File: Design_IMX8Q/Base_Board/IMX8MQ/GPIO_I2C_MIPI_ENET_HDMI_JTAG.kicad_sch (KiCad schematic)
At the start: 1 part, among them U1 MIMX8MQ6CVAHZAB

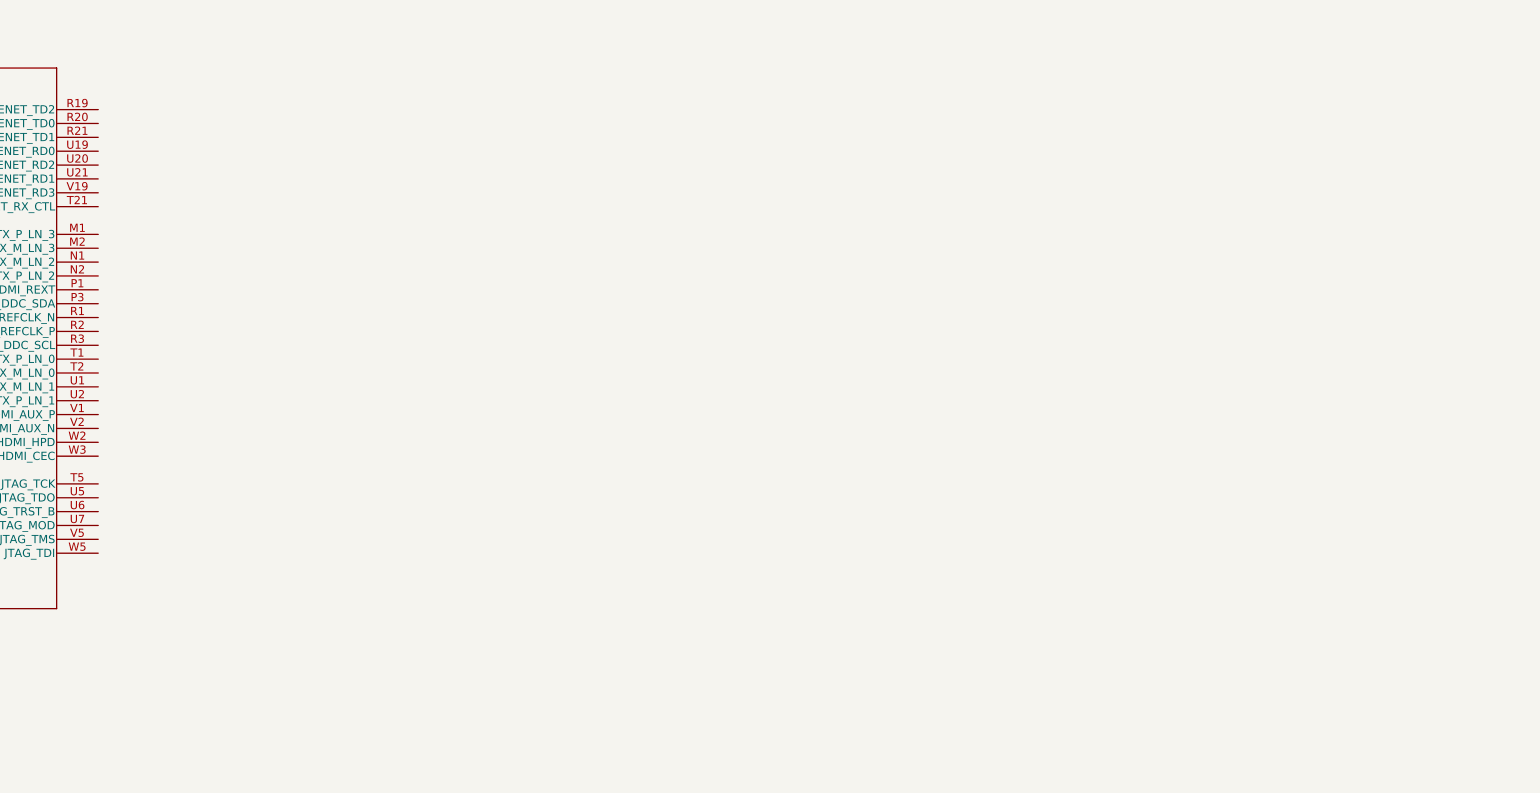
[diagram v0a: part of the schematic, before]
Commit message: changes vias pad size
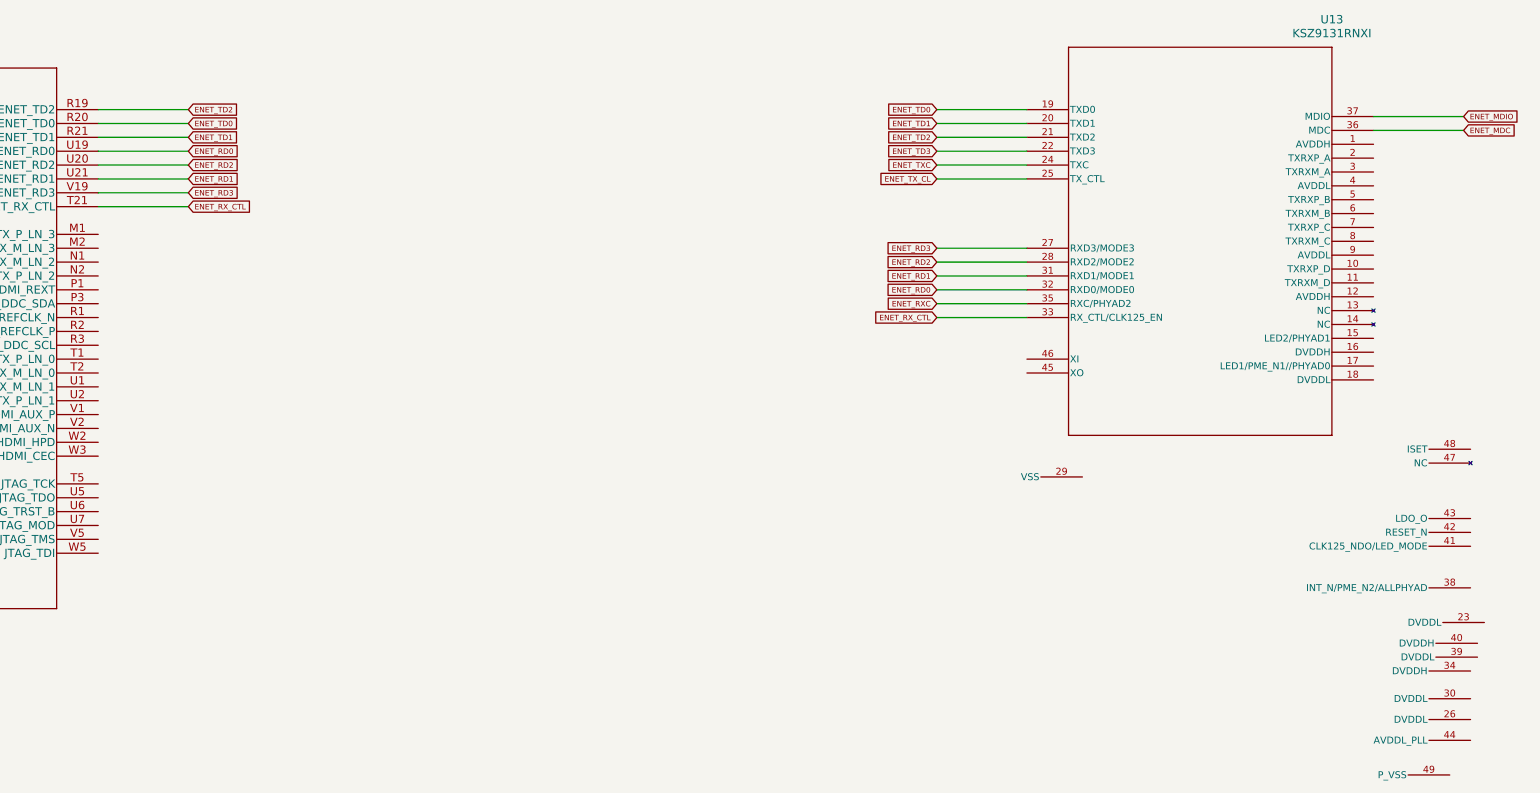
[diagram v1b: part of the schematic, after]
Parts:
- added U13: KSZ9131RNXI, Package_DFN_QFN:VQFN-48-1EP_7x7mm_P0.5mm_EP5.15x5.15mm, symbol KSZ9131RNXI:KSZ9131RNXI
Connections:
- net ENET_TD2: now reaches U1.R19 (ENET_TD2)
- net ENET_TD2: now also U13.21 (TXD2)
- net ENET_TD0: now reaches U1.R20 (ENET_TD0)
- net ENET_TD0: now also U13.19 (TXD0)
- net ENET_TD1: now reaches U1.R21 (ENET_TD1)
- net ENET_TD1: now also U13.20 (TXD1)
- net ENET_RX_CTL: now reaches U1.T21 (ENET_RX_CTL)
- net ENET_RX_CTL: now also U13.33 (RX_CTL/CLK125_EN)
- net ENET_RD0: now reaches U1.U19 (ENET_RD0)
- net ENET_RD0: now also U13.32 (RXD0/MODE0)
- net ENET_RD2: now reaches U1.U20 (ENET_RD2)
- net ENET_RD2: now also U13.28 (RXD2/MODE2)
- net ENET_RD1: now reaches U1.U21 (ENET_RD1)
- net ENET_RD1: now also U13.31 (RXD1/MODE1)
- net ENET_RD3: now reaches U1.V19 (ENET_RD3)
- net ENET_RD3: now also U13.27 (RXD3/MODE3)
- new net ENET_MDC: U13.36 (MDC)
- new net ENET_MDIO: U13.37 (MDIO)
- new net ENET_RXC: U13.35 (RXC/PHYAD2)
- new net ENET_TD3: U13.22 (TXD3)
- new net ENET_TXC: U13.24 (TXC)
- new net ENET_TX_CL: U13.25 (TX_CTL)

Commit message: Update IMX6QP and IMX8MQ
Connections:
- net MIPI_CSI2_CLK-: now reaches U1.A19 (MIPI_CSI2_CLK_N)
- net MIPI_CSI1_CLK-: now reaches U1.A22 (MIPI_CSI1_CLK_N)
- net MIPI_CSI2_CLK+: now reaches U1.B19 (MIPI_CSI2_CLK_P)
- net MIPI_CSI1_CLK+: now reaches U1.B22 (MIPI_CSI1_CLK_P)
- net MIPI_DSI_CLK-: now reaches U1.C16 (MIPI_DSI_CLK_N)
- net MIPI_DSI_REXT: now reaches U1.C17 (MIPI_DSI_REXT)
- net MIPI_DSI_CLK+: now reaches U1.D16 (MIPI_DSI_CLK_P)
- net HDMI_TX_LN_3_+: now reaches U1.M1 (HDMI_TX_P_LN_3)
- net HDMI_TX_LN_3_-: now reaches U1.M2 (HDMI_TX_M_LN_3)
- net HDMI_TX_LN_2_-: now reaches U1.N1 (HDMI_TX_M_LN_2)
- net HDMI_TX_LN_2_+: now reaches U1.N2 (HDMI_TX_P_LN_2)
- net HDMI_REXT: now reaches U1.P1 (HDMI_REXT)
- net HDMI_DDC_SDA: now reaches U1.P3 (HDMI_DDC_SDA)
- net HDMI_REFCLK_-: now reaches U1.R1 (HDMI_REFCLK_N)
- net HDMI_REFCLK_+: now reaches U1.R2 (HDMI_REFCLK_P)
- net HDMI_DDC_SCL: now reaches U1.R3 (HDMI_DDC_SCL)
- net HDMI_TX_LN_0_+: now reaches U1.T1 (HDMI_TX_P_LN_0)
- net HDMI_TX_LN_0_-: now reaches U1.T2 (HDMI_TX_M_LN_0)
- net JTAG_TCK: now reaches U1.T5 (JTAG_TCK)
- net HDMI_TX_LN_1_-: now reaches U1.U1 (HDMI_TX_M_LN_1)
- net HDMI_TX_LN_1_+: now reaches U1.U2 (HDMI_TX_P_LN_1)
- net JTAG_TDO: now reaches U1.U5 (JTAG_TDO)
- net JTAG_TRST_B: now reaches U1.U6 (JTAG_TRST_B)
- net JTAG_MOD: now reaches U1.U7 (JTAG_MOD)
- net HDMI_AUX_+: now reaches U1.V1 (HDMI_AUX_P)
- net HDMI_AUX_-: now reaches U1.V2 (HDMI_AUX_N)
- net JTAG_TMS: now reaches U1.V5 (JTAG_TMS)
- net HDMI_HPD: now reaches U1.W2 (HDMI_HPD)
- net HDMI_CEC: now reaches U1.W3 (HDMI_CEC)
- net JTAG_TDI: now reaches U1.W5 (JTAG_TDI)

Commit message: Add QSPI and more color
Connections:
- net I2C1_SCL: now reaches U1.E7 (I2C1_SCL)
- net I2C1_SDA: now reaches U1.E8 (I2C1_SDA)
- net I2C3_SDA: now reaches U1.E9 (I2C3_SDA)
- net I2C2_SDA: now reaches U1.F7 (I2C2_SDA)
- net I2C4_SCL: now reaches U1.F8 (I2C4_SCL)
- net I2C4_SDA: now reaches U1.F9 (I2C4_SDA)
- net I2C2_SCL: now reaches U1.G7 (I2C2_SCL)
- net I2C3_SCL: now reaches U1.G8 (I2C3_SCL)
- net USB1_OTG_OC: now reaches U1.K6 (GPIO1_IO13)
- net USB1_OTG_PWR: now reaches U1.L7 (GPIO1_IO12)
- net USB1_OTG_ID: now reaches U1.M7 (GPIO1_IO10)

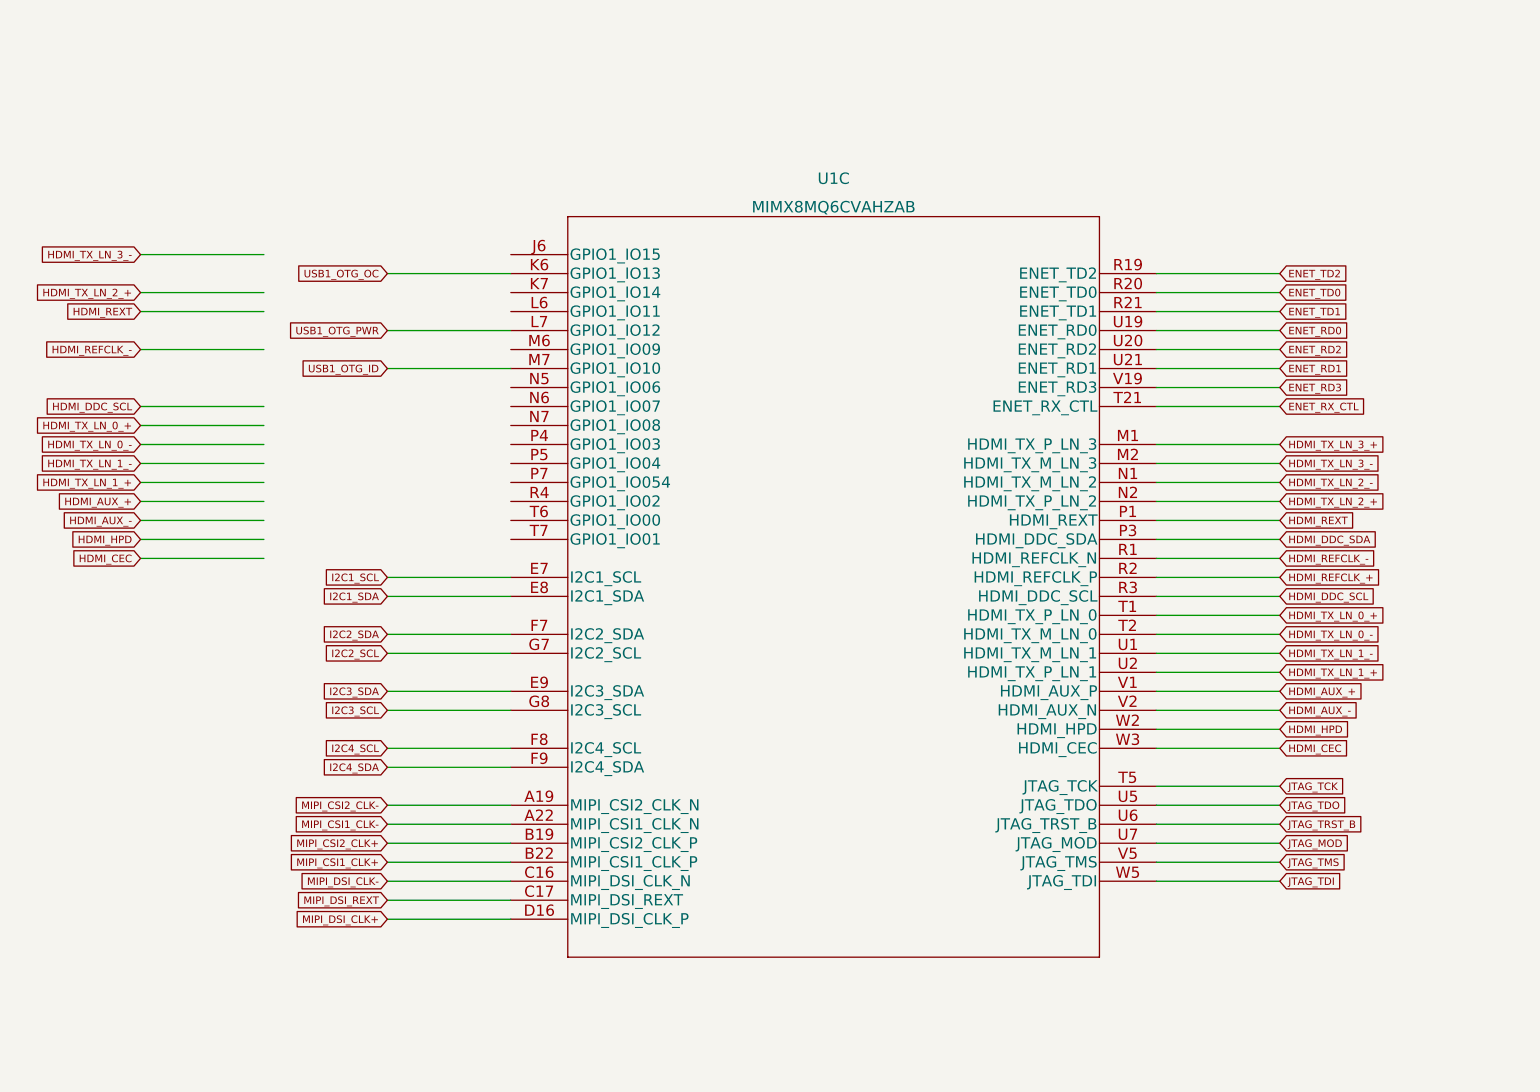
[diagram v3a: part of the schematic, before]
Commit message: it was inserted power control system
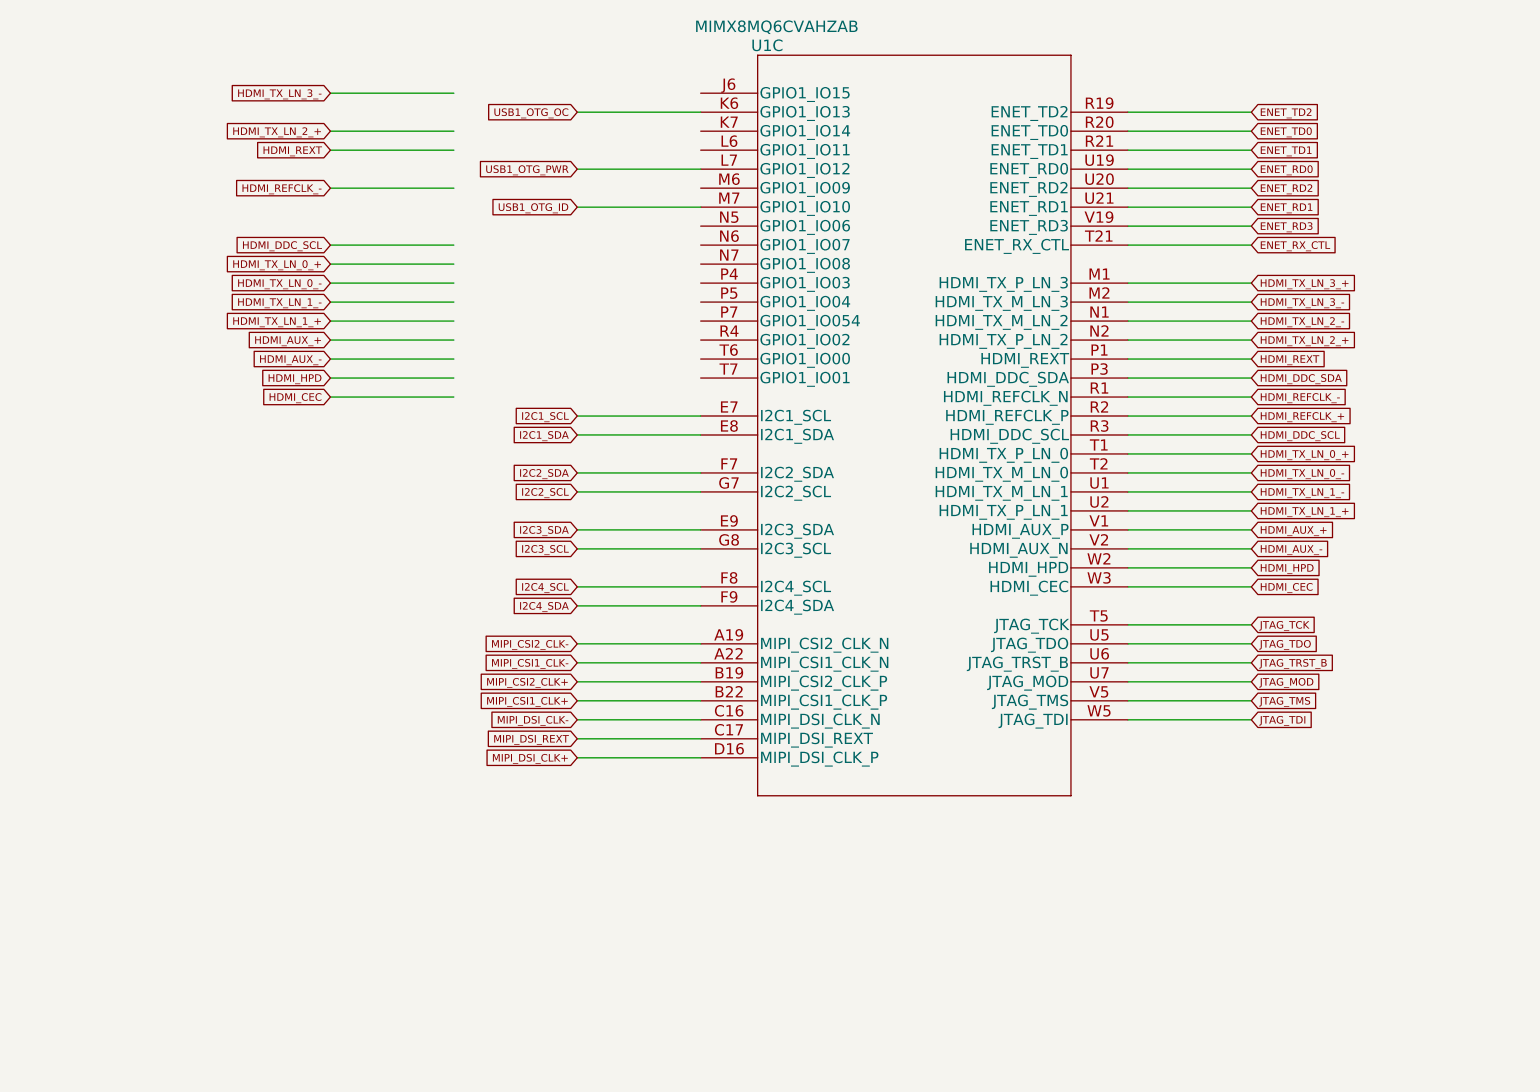
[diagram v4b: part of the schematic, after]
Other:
- moved on the sheet: U1C
